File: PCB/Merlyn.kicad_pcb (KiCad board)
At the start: 2 copper layers, 35 x 35 mm, 46 parts, among them Q1 JMSL0302AU, Q10 JMSL0302AU, Q11 JMSL0302AU, Q12 JMSL0302AU, Q13 JMSL0302AU, Q14 JMSL0302AU, Q15 JMSL0302AU, Q16 JMSL0302AU, Q17 JMSL0302AU, Q18 JMSL0302AU, Q19 JMSL0302AU, Q2 JMSL0302AU, Q20 JMSL0302AU, Q21 JMSL0302AU, Q22 JMSL0302AU, Q23 JMSL0302AU, Q24 JMSL0302AU, Q3 JMSL0302AU, Q4 JMSL0302AU, Q5 JMSL0302AU, Q6 JMSL0302AU, Q7 JMSL0302AU, Q8 JMSL0302AU, Q9 JMSL0302AU, U1 AT32F435CGU7, U10 JSM6288Q, U11 EFM8BB21F16G-C-QFN20, U12 EFM8BB21F16G-C-QFN20, U13 EFM8BB21F16G-C-QFN20, U14 JSM6288Q, U15 JSM6288Q, U16 JSM6288Q, U17 MPU6500, U2 ESP8285H16, U3 LMR51420YDDCR, U4 SPX3819M5-L-3-3/TR, U5 SX1281IMLTRT, U6 W25Q128JVPIM TR, U7 APH0420T4R7M, U8 AT7456E, U9 EFM8BB21F16G-C-QFN20, X1 TAXM8M4RDBCCT2T, X2 7D027000I01, X3 XL7EL89CMI-111YLC-26M, X4 XC21M4-52.000-F10NNHPL

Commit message: routing checkpoint
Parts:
- removed Q10, Q11, Q12, Q13, Q14, Q15, Q16, Q17, Q18, Q19, Q2, Q20, Q21, Q22, Q23, Q24, Q3, Q4, Q5, Q6, Q7, Q8, Q9: JMSL0302AU, easyeda2kicad:DFN-8_L3.2-W3.1-P0.65-LS3.4-BL
- removed U10, U14, U15, U16: JSM6288Q, easyeda2kicad:VQFN-24_L4.0-W4.0-P0.50-TL-EP2.7
- removed U11, U12, U13, U9: EFM8BB21F16G-C-QFN20, easyeda2kicad:QFN-20_L3.0-W3.0-P0.50-BL-EP1.7_EFM8BB21F16G
- added C1: 0.1uF, Capacitor_SMD:C_0402_1005Metric, F.Cu at (77.3, 52.4)
- added C10: 0.1uF, Capacitor_SMD:C_0402_1005Metric, F.Cu at (137.2, 74.8)
- added C11: 0.1uF, Capacitor_SMD:C_0402_1005Metric, F.Cu at (137.2, 76.4)
- added C12: 10uF, Capacitor_SMD:C_0402_1005Metric, F.Cu at (77.3, 64.2)
- added C13: 0.1uF, Capacitor_SMD:C_0402_1005Metric, F.Cu at (77.3, 66.2)
- added C14: 0.1uF, Capacitor_SMD:C_0402_1005Metric, F.Cu at (80.2, 52.4)
- added C15: 0.1uF, Capacitor_SMD:C_0402_1005Metric, F.Cu at (80.2, 54.4)
- added C16: 10pF, Capacitor_SMD:C_0402_1005Metric, F.Cu at (80.2, 56.4)
- added C17: 10pF, Capacitor_SMD:C_0402_1005Metric, F.Cu at (80.2, 58.3)
- added C18: 10nF, Capacitor_SMD:C_0402_1005Metric, F.Cu at (143.9, 81.8)
- added C19: 0.1uF, Capacitor_SMD:C_0402_1005Metric, F.Cu at (80.2, 62.3)
- added C2: 10uF, Capacitor_SMD:C_0603_1608Metric, F.Cu at (89.4, 52.7)
- added C20: 10nF, Capacitor_SMD:C_0402_1005Metric, F.Cu at (144.4, 80.7)
- added C21: 470nF, Capacitor_SMD:C_0402_1005Metric, F.Cu at (146.6, 81.8)
- added C22: 0.1uF, Capacitor_SMD:C_0402_1005Metric, F.Cu at (83.1, 52.4)
- added C23: 10uF, Capacitor_SMD:C_0402_1005Metric, F.Cu at (83.1, 54.4)
- added C24: 0.1uF, Capacitor_SMD:C_0402_1005Metric, F.Cu at (83.1, 56.4)
- added C25: 0.1uF, Capacitor_SMD:C_0402_1005Metric, F.Cu at (145.7, 67.8)
- added C26: 0.1uF, Capacitor_SMD:C_0402_1005Metric, F.Cu at (138.0, 60.7)
- added C27: 22uF, Capacitor_SMD:C_0805_2012Metric, F.Cu at (145.8, 62.0)
- added C28: 22uF, Capacitor_SMD:C_0805_2012Metric, F.Cu at (148.5, 67.5)
- added C29: 0.1uF, Capacitor_SMD:C_0402_1005Metric, F.Cu at (145.2, 64.8)
- added C3: 10uF, Capacitor_SMD:C_0603_1608Metric, F.Cu at (89.4, 55.2)
- added C30: 0.1uF, Capacitor_SMD:C_0402_1005Metric, F.Cu at (145.7, 66.7)
- added C31: 10pF, Capacitor_SMD:C_0402_1005Metric, F.Cu at (128.5, 79.9)
- added C32: 10pF, Capacitor_SMD:C_0402_1005Metric, F.Cu at (133.6, 79.9)
- added C33: 0.1uF, Capacitor_SMD:C_0402_1005Metric, F.Cu at (134.0, 78.3)
- added C34: 0.1uF, Capacitor_SMD:C_0402_1005Metric, F.Cu at (127.2, 76.0)
- added C35: 0.1uF, Capacitor_SMD:C_0402_1005Metric, F.Cu at (128.9, 69.3)
- added C36: 0.1uF, Capacitor_SMD:C_0402_1005Metric, F.Cu at (136.0, 70.3)
- added C37: 0.1uF, Capacitor_SMD:C_0402_1005Metric, F.Cu at (85.9, 62.3)
- added C38: 10uF, Capacitor_SMD:C_0402_1005Metric, F.Cu at (85.9, 64.2)
- added C39: 0.1uF, Capacitor_SMD:C_0402_1005Metric, F.Cu at (85.9, 66.2)
- added C4: 4.7uF, Capacitor_SMD:C_1206_3216Metric, F.Cu at (83.3, 80.1)
- added C40: 0.1uF, Capacitor_SMD:C_0402_1005Metric, F.Cu at (104.8, 61.5)
- added C41: 0.1uF, Capacitor_SMD:C_0402_1005Metric, F.Cu at (104.8, 63.4)
- added C5: 0.1uF, Capacitor_SMD:C_0402_1005Metric, F.Cu at (77.3, 54.4)
- added C6: 10uF, Capacitor_SMD:C_0603_1608Metric, F.Cu at (89.4, 57.7)
- added C7: 10uF, Capacitor_SMD:C_0603_1608Metric, F.Cu at (89.4, 60.2)
- added C8: 10nF, Capacitor_SMD:C_0402_1005Metric, F.Cu at (77.3, 56.4)
- added C9: 10nF, Capacitor_SMD:C_0402_1005Metric, F.Cu at (139.3, 76.4)
- added D1: USBLC6-2SC6, easyeda2kicad:SOT-23-6_L2.9-W1.6-P0.95-LS2.8-BL, B.Cu at (78.3, 80.6)
- added D2: RED, easyeda2kicad:LED0805-RD, F.Cu at (109.0, 65.0)
- added D3: GREEN, easyeda2kicad:LED0805-R-RD, F.Cu at (109.1, 61.7)
- added D4: 1N4148W, Diode_SMD:D_SOD-123, B.Cu at (83.4, 83.5)
- added FL1: 2450FM07D0034T, easyeda2kicad:FIL_2450FM07D0034T, F.Cu at (141.1, 83.4)
- added H1: ~, easyeda2kicad:Buzzer Pad, F.Cu at (120.2, 61.4)
- added H2: ~, easyeda2kicad:JST_SH_SM08B-SRSS-TB_1x08-1MP_P1.00mm_Horizontal, F.Cu at (149.9, 74.2)
- added H3: ~, easyeda2kicad:Camera Pad, F.Cu at (142.0, 59.9)
- added J1: Conn_Coaxial_Small, easyeda2kicad:UFL, F.Cu at (144.2, 84.8)
- added R10: 5.1k, Resistor_SMD:R_0402_1005Metric, F.Cu at (95.7, 60.4)
- added R11: 5.1k, Resistor_SMD:R_0402_1005Metric, F.Cu at (98.6, 52.4)
- added R12: 75, Resistor_SMD:R_0402_1005Metric, F.Cu at (138.0, 59.6)
- added R13: 75, Resistor_SMD:R_0402_1005Metric, F.Cu at (147.5, 60.4)
- added R14: 12k, Resistor_SMD:R_0402_1005Metric, F.Cu at (98.6, 58.4)
- added R15: 12k, Resistor_SMD:R_0402_1005Metric, F.Cu at (98.6, 60.4)
- added R16: 12k, Resistor_SMD:R_0402_1005Metric, F.Cu at (101.6, 52.4)
- added R17: 5.1k, Resistor_SMD:R_0402_1005Metric, F.Cu at (101.6, 54.4)
- added R18: 5.1k, Resistor_SMD:R_0402_1005Metric, F.Cu at (101.6, 56.4)
- added R19: 12k, Resistor_SMD:R_0402_1005Metric, F.Cu at (101.6, 58.4)
- added R2: 15k, Resistor_SMD:R_0402_1005Metric, F.Cu at (92.8, 54.4)
- added R20: 1.5k, Resistor_SMD:R_0402_1005Metric, F.Cu at (101.6, 60.4)
- added R21: 5.1k, Resistor_SMD:R_0402_1005Metric, F.Cu at (129.5, 67.2)
- added R22: 5.1k, Resistor_SMD:R_0402_1005Metric, F.Cu at (131.6, 67.0)
- added R3: 2k, Resistor_SMD:R_0402_1005Metric, F.Cu at (92.8, 56.4)
- added R4: 12k, Resistor_SMD:R_0402_1005Metric, F.Cu at (92.8, 58.4)
- added R5: 0, Resistor_SMD:R_0402_1005Metric, F.Cu at (92.8, 60.4)
- added R6: 12k, Resistor_SMD:R_0402_1005Metric, F.Cu at (95.7, 52.4)
- added R7: 0, Resistor_SMD:R_0402_1005Metric, F.Cu at (95.7, 54.4)
- added R8: 12k, Resistor_SMD:R_0402_1005Metric, F.Cu at (95.7, 56.4)
- added R9: 12k, Resistor_SMD:R_0402_1005Metric, F.Cu at (95.7, 58.4)
- added REF**: MountingHole, easyeda2kicad:MountingHole, F.Cu at (129.5, 84.0)
- added REF**: MountingHole, easyeda2kicad:MountingHole, F.Cu at (149.5, 64.0)
- added REF**: MountingHole, easyeda2kicad:MountingHole, F.Cu at (149.5, 84.0)
- added REF**: MountingHole, easyeda2kicad:MountingHole, F.Cu at (129.5, 64.0)
- added U18: LMR51420, easyeda2kicad:SOT-23-6_L2.9-W1.6-P0.95-LS2.9-BL, F.Cu at (109.1, 77.9)
- added USB1: TYPE-C 16PIN 2MD(073), easyeda2kicad:USB-C-SMD_TYPE-C-6PIN-2MD-073, B.Cu at (125.8, 51.3)
- Q1: value JMSL0302AU -> 2N7002; footprint easyeda2kicad:DFN-8_L3.2-W3.1-P0.65-LS3.4-BL -> Package_TO_SOT_SMD:SOT-23
- R1: value HOYLR2512E-3W-0.5MR-1% -> 12k; footprint easyeda2kicad:R2512 -> Resistor_SMD:R_0402_1005Metric; moved to F.Cu
- U3: value LMR51420YDDCR -> W25Q128JVSIQTR; footprint easyeda2kicad:SOT-23-6_L2.9-W1.6-P0.95-LS2.9-BL -> easyeda2kicad:SOIC-8_L5.3-W5.3-P1.27-LS8.0-BL; moved to B.Cu
- U4: value SPX3819M5-L-3-3/TR -> SPX3819; moved to B.Cu
- U6: value W25Q128JVPIM TR -> BMP388; footprint easyeda2kicad:WSON-8_L6.0-W5.0-P1.27-BL-EP -> easyeda2kicad:LGA-10_L2.0-W2.0-P0.50-BL
- U7: value APH0420T4R7M -> 4.7uH
- X1: value TAXM8M4RDBCCT2T -> 8MHz
- X2: value 7D027000I01 -> 27MHz
- X3: value XL7EL89CMI-111YLC-26M -> 26MHz
- X4: value XC21M4-52.000-F10NNHPL -> 52MHz
- moved Q1 45.4 mm to (108.9, 72.2), turned to 180 degrees
- moved R1 42.7 mm to (92.8, 52.4)
- moved U7 29.9 mm to (103.4, 78.5)
- moved X3 23.3 mm to (136.2, 80.8)
- moved U8 21.6 mm to (140.8, 66.1), turned to -90 degrees
- moved X4 19.1 mm to (146.5, 79.9), turned to 90 degrees
- moved U5 16.8 mm to (140.8, 79.9), turned to 180 degrees
- moved U2 16.7 mm to (135.6, 85.6)
- moved X2 14.8 mm to (135.7, 64.7), turned to 90 degrees
- moved U1 13.1 mm to (131.6, 73.7), turned to 90 degrees
- moved U6 12.2 mm to (133.3, 64.7)
- moved U4 9.40 mm to (133.0, 72.4), turned to 180 degrees
- moved U17 7.66 mm to (139.5, 74.0), turned to 180 degrees
- moved U3 1.91 mm to (127.8, 75.4), turned to 180 degrees
- moved X1 0.76 mm to (131.0, 80.0), turned to 180 degrees
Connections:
- Q1 pad 1: unconnected-(Q1-S-Pad1) -> Net-(Q1-G)
- Q1 pad 2: unconnected-(Q1-S-Pad2) -> GND
- Q1 pad 3: unconnected-(Q1-S-Pad3) -> Net-(D4-A)
- R1 pad 1: unconnected-(R1-Pad1) -> +3V3
- R1 pad 2: unconnected-(R1-Pad2) -> NRST
- U1 pad 1: unconnected-(U1-VBAT-Pad1) -> +3V3
- U1 pad 10: unconnected-(U1-PA0-Pad10) -> ADC_VOL
- U1 pad 11: unconnected-(U1-PA1-Pad11) -> ADC_CUR
- U1 pad 12: unconnected-(U1-PA2-Pad12) -> UART2_TX
- U1 pad 13: unconnected-(U1-PA3-Pad13) -> UART2_RX
- U1 pad 14: unconnected-(U1-PA4-Pad14) -> SPI1_CS
- U1 pad 15: unconnected-(U1-PA5-Pad15) -> SPI1_SCK
- U1 pad 16: unconnected-(U1-PA6-Pad16) -> SPI1_MISO
- U1 pad 17: unconnected-(U1-PA7-Pad17) -> SPI1_MOSI
- U1 pad 18: unconnected-(U1-PB0-Pad18) -> MOT3
- U1 pad 19: unconnected-(U1-PB1-Pad19) -> MOT4
- U1 pad 2: unconnected-(U1-PC13-Pad2) -> SPI2_CS2
- U1 pad 20: unconnected-(U1-PB2-Pad20) -> BOOT1
- U1 pad 21: unconnected-(U1-PB10-Pad21) -> UART3_TX
- U1 pad 22: unconnected-(U1-PB11-Pad22) -> UART3_RX
- U1 pad 23: unconnected-(U1-PH3-Pad23) -> I2C_SDA
- U1 pad 24: unconnected-(U1-VDD-Pad24) -> +3V3
- U1 pad 25: unconnected-(U1-PB12-Pad25) -> SPI2_CS1
- U1 pad 26: unconnected-(U1-PB13-Pad26) -> SPI2_SCK
- U1 pad 27: unconnected-(U1-PB14-Pad27) -> SPI2_MISO
- U1 pad 28: unconnected-(U1-PB15-Pad28) -> SPI2_MOSI
- U1 pad 29: unconnected-(U1-PA8-Pad29) -> LED
- U1 pad 30: unconnected-(U1-PA9-Pad30) -> UART1_TX
- U1 pad 31: unconnected-(U1-PA10-Pad31) -> UART1_RX
- U1 pad 32: unconnected-(U1-PA11-Pad32) -> D-
- U1 pad 33: unconnected-(U1-PA12-Pad33) -> D+
- U1 pad 34: unconnected-(U1-PA13-Pad34) -> SWDIO
- U1 pad 35: unconnected-(U1-PH2-Pad35) -> I2C_SCL
- U1 pad 36: unconnected-(U1-VDD-Pad36) -> +3V3
- U1 pad 37: unconnected-(U1-PA14-Pad37) -> SWCLK
- U1 pad 39: unconnected-(U1-PB3-Pad39) -> UART7_RX
- U1 pad 4: unconnected-(U1-PC15-Pad4) -> BEEPER
- U1 pad 40: unconnected-(U1-PB4-Pad40) -> UART7_TX
- U1 pad 42: unconnected-(U1-PB6-Pad42) -> MOT1
- U1 pad 43: unconnected-(U1-PB7-Pad43) -> MOT2
- U1 pad 44: unconnected-(U1-BOOT0-Pad44) -> BOOT0
- U1 pad 45: unconnected-(U1-PB8-Pad45) -> UART5_RX
- U1 pad 46: unconnected-(U1-PB9-Pad46) -> UART5_TX
- U1 pad 47: unconnected-(U1-VSS-Pad47) -> GND
- U1 pad 48: unconnected-(U1-VDD-Pad48) -> +3V3
- U1 pad 49: unconnected-(U1-EP-Pad49) -> GND
- U1 pad 5: unconnected-(U1-PH0-Pad5) -> Net-(U1-PH0)
- U1 pad 6: unconnected-(U1-PH1-Pad6) -> Net-(U1-PH1)
- U1 pad 7: unconnected-(U1-NRST-Pad7) -> NRST
- U1 pad 8: unconnected-(U1-VSSA/VREF--Pad8) -> GND
- U1 pad 9: unconnected-(U1-VDDA/VREF+-Pad9) -> +3V3
- U17 pad 10: unconnected-(U17-REGOUT-Pad10) -> Net-(U17-REGOUT)
- U17 pad 11: unconnected-(U17-FSYNC-Pad11) -> GND
- U17 pad 13: unconnected-(U17-VDD-Pad13) -> +3V3
- U17 pad 18: unconnected-(U17-GND-Pad18) -> GND
- U17 pad 20: unconnected-(U17-RESV-Pad20) -> GND
- U17 pad 22: unconnected-(U17-nCS-Pad22) -> SPI1_CS
- U17 pad 23: unconnected-(U17-SCL/SCLK-Pad23) -> SPI1_SCK
- U17 pad 24: unconnected-(U17-SDA/SDI-Pad24) -> SPI1_MOSI
- U17 pad 8: unconnected-(U17-VDDIO-Pad8) -> +3V3
- U17 pad 9: unconnected-(U17-SDO/AD0-Pad9) -> SPI1_MISO
- U2 pad 1: unconnected-(U2-VDDA-Pad1) -> +3V3
- U2 pad 10: unconnected-(U2-MTDI-Pad10) -> GPIO12
- U2 pad 11: unconnected-(U2-VDDPST-Pad11) -> +3V3
- U2 pad 12: unconnected-(U2-MTCK-Pad12) -> GPIO13
- U2 pad 13: unconnected-(U2-MTDO-Pad13) -> GPIO15
- U2 pad 14: unconnected-(U2-GPIO2-Pad14) -> GPIO2
- U2 pad 15: unconnected-(U2-GPIO0-Pad15) -> Net-(U2-GPIO0)
- U2 pad 16: unconnected-(U2-GPIO4-Pad16) -> GPIO4
- U2 pad 17: unconnected-(U2-VDDPST-Pad17) -> +3V3
- U2 pad 24: unconnected-(U2-GPIO5-Pad24) -> GPIO5
- U2 pad 25: unconnected-(U2-U0RXD-Pad25) -> PIN
- U2 pad 26: unconnected-(U2-U0TXD-Pad26) -> PIN
- U2 pad 27: unconnected-(U2-XTAL_OUT-Pad27) -> Net-(U2-XTAL_OUT)
- U2 pad 28: unconnected-(U2-XTAL_IN-Pad28) -> Net-(U2-XTAL_IN)
- U2 pad 29: unconnected-(U2-VDDD-Pad29) -> +3V3
- U2 pad 3: unconnected-(U2-VDD3P3-Pad3) -> +3V3
- U2 pad 30: unconnected-(U2-VDDA-Pad30) -> +3V3
- U2 pad 31: unconnected-(U2-RES12K-Pad31) -> Net-(U2-RES12K)
- U2 pad 33: unconnected-(U2-GND-Pad33) -> GND
- U2 pad 4: unconnected-(U2-VDD3P3-Pad4) -> +3V3
- U2 pad 7: unconnected-(U2-CHIP_EN-Pad7) -> Net-(U2-CHIP_EN)
- U2 pad 9: unconnected-(U2-MTMS-Pad9) -> GPIO14
- U3 pad 1: unconnected-(U3-GND-Pad1) -> PIN
- U3 pad 2: unconnected-(U3-SW-Pad2) -> PIN
- U3 pad 3: unconnected-(U3-VIN-Pad3) -> +3V3
- U3 pad 4: unconnected-(U3-FB-Pad4) -> GND
- U3 pad 5: unconnected-(U3-EN-Pad5) -> PIN
- U3 pad 6: unconnected-(U3-CB-Pad6) -> PIN
- U4 pad 1: unconnected-(U4-IN-Pad1) -> +5V
- U4 pad 2: unconnected-(U4-GND-Pad2) -> GND
- U4 pad 3: unconnected-(U4-EN-Pad3) -> +5V
- U4 pad 4: unconnected-(U4-BYP-Pad4) -> Net-(U4-BYP)
- U4 pad 5: unconnected-(U4-OUT-Pad5) -> +3V3
- U5 pad 1: unconnected-(U5-VR_PA-Pad1) -> Net-(U5-VR_PA)
- U5 pad 11: unconnected-(U5-VBAT_IO-Pad11) -> +3V3
- U5 pad 12: unconnected-(U5-DCC_FB-Pad12) -> DCC_FB
- U5 pad 13: unconnected-(U5-GND-Pad13) -> GND
- U5 pad 15: unconnected-(U5-VBAT-Pad15) -> +3V3
- U5 pad 16: unconnected-(U5-MISO_TX-Pad16) -> GPIO12
- U5 pad 17: unconnected-(U5-MOSI_RX-Pad17) -> GPIO13
- U5 pad 18: unconnected-(U5-SCK_RTSN-Pad18) -> GPIO14
- U5 pad 19: unconnected-(U5-NSS_CTS-Pad19) -> GPIO15
- U5 pad 2: unconnected-(U5-VDD_IN-Pad2) -> DCC_FB
- U5 pad 20: unconnected-(U5-GND-Pad20) -> GND
- U5 pad 21: unconnected-(U5-GND-Pad21) -> GND
- U5 pad 22: unconnected-(U5-RFIO-Pad22) -> RFOUT
- U5 pad 23: unconnected-(U5-GND-Pad23) -> GND
- U5 pad 24: unconnected-(U5-GND-Pad24) -> GND
- U5 pad 25: unconnected-(U5-EP-Pad25) -> GND
- U5 pad 3: unconnected-(U5-NRESET-Pad3) -> GPIO2
- U5 pad 4: unconnected-(U5-XTA-Pad4) -> Net-(U5-XTA)
- U5 pad 5: unconnected-(U5-GND-Pad5) -> GND
- U5 pad 6: unconnected-(U5-XTB-Pad6) -> Net-(U5-XTB)
- U5 pad 7: unconnected-(U5-BUSY-Pad7) -> GPIO5
- U5 pad 8: unconnected-(U5-DIO1-Pad8) -> GPIO4
- U6 pad 1: unconnected-(U6-/CS-Pad1) -> +3V3
- U6 pad 2: unconnected-(U6-DO(IO1)-Pad2) -> I2C_SCL
- U6 pad 3: unconnected-(U6-/WP(IO2)-Pad3) -> GND
- U6 pad 4: unconnected-(U6-GND-Pad4) -> I2C_SDA
- U6 pad 5: unconnected-(U6-DI(IO0)-Pad5) -> GND
- U6 pad 6: unconnected-(U6-CLK-Pad6) -> +3V3
- U6 pad 8: unconnected-(U6-VCC-Pad8) -> GND
- U6 pad 9: unconnected-(U6-EP-Pad9) -> GND
- U7 pad 1: unconnected-(U7-Pad1) -> Net-(U18-SW)
- U7 pad 2: unconnected-(U7-Pad2) -> +5V
- U8 pad 10: unconnected-(U8-SCLK-Pad10) -> SPI2_SCK
- U8 pad 11: unconnected-(U8-SDOUT-Pad11) -> SPI2_MISO
- U8 pad 19: unconnected-(U8-~{RESET}-Pad19) -> +5V
- U8 pad 20: unconnected-(U8-AGND-Pad20) -> GND
- U8 pad 21: unconnected-(U8-AVDD-Pad21) -> +5V
- U8 pad 22: unconnected-(U8-VIN-Pad22) -> VIN
- U8 pad 23: unconnected-(U8-PGND-Pad23) -> GND
- U8 pad 24: unconnected-(U8-PVDD-Pad24) -> +5V
- U8 pad 25: unconnected-(U8-SAG-Pad25) -> Net-(U8-SAG)
- U8 pad 26: unconnected-(U8-VOUT-Pad26) -> Net-(U8-VOUT)
- U8 pad 29: unconnected-(U8-EP-Pad29) -> GND
- U8 pad 3: unconnected-(U8-DVDD-Pad3) -> +5V
- U8 pad 4: unconnected-(U8-DGND-Pad4) -> GND
- U8 pad 5: unconnected-(U8-CLKIN-Pad5) -> Net-(U8-CLKIN)
- U8 pad 6: unconnected-(U8-XFB-Pad6) -> Net-(U8-XFB)
- U8 pad 8: unconnected-(U8-~{CS}-Pad8) -> SPI2_CS1
- U8 pad 9: unconnected-(U8-SDIN-Pad9) -> SPI2_MOSI
- X1 pad 1: unconnected-(X1-Pad1) -> Net-(U1-PH1)
- X1 pad 2: unconnected-(X1-Pad2) -> GND
- X1 pad 3: unconnected-(X1-Pad3) -> Net-(U1-PH0)
- X1 pad 4: unconnected-(X1-Pad4) -> GND
- X2 pad 1: unconnected-(X2-Pad1) -> Net-(U8-XFB)
- X2 pad 2: unconnected-(X2-GND-Pad2) -> GND
- X2 pad 3: unconnected-(X2-Pad3) -> Net-(U8-CLKIN)
- X2 pad 4: unconnected-(X2-GND-Pad4) -> GND
- X3 pad 1: unconnected-(X3-Pad1) -> Net-(U2-XTAL_IN)
- X3 pad 2: unconnected-(X3-GND-Pad2) -> GND
- X3 pad 3: unconnected-(X3-Pad3) -> Net-(U2-XTAL_OUT)
- X3 pad 4: unconnected-(X3-GND-Pad4) -> GND
- X4 pad 1: unconnected-(X4-Pad1) -> Net-(U5-XTA)
- X4 pad 2: unconnected-(X4-GND-Pad2) -> GND
- X4 pad 3: unconnected-(X4-Pad3) -> Net-(U5-XTB)
- X4 pad 4: unconnected-(X4-GND-Pad4) -> GND
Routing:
- net GND: track 0.00 -> 33.3 mm, vias 0 -> 45
- net DCC_FB: track 0.00 -> 13.0 mm, vias 0 -> 2
- net +3V3: track 0.00 -> 10.6 mm, vias 0 -> 5
- net Net-(C27-Pad1): track 0.00 -> 9.67 mm
- net SPI1_SCK: track 0.00 -> 9.08 mm, vias 0 -> 2
- net VIN: track 0.00 -> 8.98 mm
- net SPI1_CS: track 0.00 -> 8.94 mm, vias 0 -> 2
- net SPI1_MOSI: track 0.00 -> 8.61 mm, vias 0 -> 2
- net SPI2_MOSI: track 0.00 -> 7.35 mm
- net SPI2_CS1: track 0.00 -> 6.83 mm, vias 0 -> 2
- net Net-(U8-SAG): track 0.00 -> 6.73 mm
- net SPI2_MISO: track 0.00 -> 6.35 mm
- net +5V: track 0.00 -> 6.15 mm
- net SPI2_SCK: track 0.00 -> 6.13 mm, vias 0 -> 2
- net Net-(U1-PH0): track 0.00 -> 6.04 mm
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- added copper zone on In1.Cu, net +3V3
- added copper zone on B.Cu, net GND
- added copper zone on F.Cu, net GND
- added copper zone on In2.Cu, net GND
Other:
- board size 35 x 35 mm -> 30.5 x 30.5 mm
- copper layers 2 -> 4

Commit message: checkpoint
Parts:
- C2, C3, C4, R5, R7, U7: moved to B.Cu
- H2: footprint easyeda2kicad:JST_SH_SM08B-SRSS-TB_1x08-1MP_P1.00mm_Horizontal -> easyeda2kicad:ESC Header
- USB1: footprint easyeda2kicad:USB-C-SMD_TYPE-C-6PIN-2MD-073 -> easyeda2kicad:USB-TYPE-C-SMD_TYPE-C-16P-QTWT
- moved C23 69.5 mm to (151.3, 67.7)
- moved C24 69.0 mm to (151.3, 66.7)
- moved D1 64.8 mm to (142.2, 69.5), turned to -90 degrees
- moved C19 62.8 mm to (141.3, 76.4), turned to -135 degrees
- moved C14 61.3 mm to (131.4, 86.1), turned to 45 degrees
- moved C22 60.5 mm to (137.9, 78.0), turned to -90 degrees
- moved C15 60.2 mm to (134.1, 81.2), turned to 180 degrees
- moved C17 59.7 mm to (136.4, 78.4)
- moved C16 59.2 mm to (134.6, 79.7), turned to -90 degrees
- moved C5 58.6 mm to (135.7, 59.5)
- moved R11 57.7 mm to (149.2, 80.2)
- moved R10 57.4 mm to (149.2, 81.2)
- moved C1 56.0 mm to (132.4, 62.5), turned to 90 degrees
- moved R7 53.9 mm to (137.8, 88.2)
- moved R8 52.9 mm to (139.2, 86.6), turned to -90 degrees
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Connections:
- D1 pad 1: DIN+ -> DIN-
- D1 pad 3: DIN- -> DIN+
- D1 pad 4: D- -> D+
- D1 pad 6: D+ -> D-
- R16 pad 2: PIN -> SPI2_CS2
- U2 pad 25: PIN -> UART2_TX
- U2 pad 26: PIN -> UART2_RX
- U3 pad 1: PIN -> SPI2_CS2
- U3 pad 2: PIN -> SPI2_MISO
- U3 pad 5: PIN -> SPI2_MOSI
- U3 pad 6: PIN -> SPI2_SCK
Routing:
- net +3V3: track 10.6 -> 52.2 mm, vias 5 -> 14
- net +5V: track 6.15 -> 47.5 mm, vias 0 -> 6
- net SPI2_CS2: track 0.00 -> 25.1 mm, vias 0 -> 2
- net GPIO4: track 0.00 -> 18.5 mm, vias 0 -> 2
- net GND: track 33.3 -> 50.3 mm, vias 45 -> 72
- net VBAT: track 0.00 -> 14.0 mm, vias 0 -> 3
- net GPIO15: track 0.00 -> 13.8 mm, vias 0 -> 2
- net Net-(USB1-CC1): track 0.00 -> 13.5 mm, vias 0 -> 1
- net GPIO12: track 0.00 -> 13.4 mm, vias 0 -> 2
- net GPIO2: track 1.60 -> 15.0 mm, vias 1 -> 2
- net D+: track 0.00 -> 12.7 mm, vias 0 -> 1
- net D-: track 0.00 -> 12.7 mm, vias 0 -> 1
- net GPIO5: track 0.00 -> 12.4 mm, vias 0 -> 2
- net SPI2_MISO: track 6.35 -> 18.0 mm, vias 0 -> 1
- net GPIO13: track 0.00 -> 11.6 mm, vias 0 -> 2
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- added copper zone on In2.Cu, net +3V3
- added copper zone on In1.Cu, net GND
- removed copper zone on In1.Cu, net +3V3
- removed copper zone on In2.Cu, net GND

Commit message: checkpoint
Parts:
- added C42: 0.1uF, Capacitor_SMD:C_0402_1005Metric, F.Cu at (145.5, 74.7)
- added H4: ~, easyeda2kicad:VTX Pad, B.Cu at (142.8, 59.9)
- added R23: 91k, Resistor_SMD:R_0603_1608Metric, F.Cu at (144.9, 76.0)
- added R25: 12k, Resistor_SMD:R_0402_1005Metric, F.Cu at (144.1, 74.3)
- moved C39 66.8 mm to (152.7, 67.2), turned to 90 degrees
- moved C38 66.4 mm to (152.3, 65.7), turned to 180 degrees
- moved C8 65.5 mm to (141.1, 71.5), turned to 180 degrees
- moved C6 59.0 mm to (144.9, 77.5), turned to 180 degrees
- moved R17 58.0 mm to (152.4, 82.3)
- moved C7 56.3 mm to (144.6, 71.5), turned to 180 degrees
- moved R16 54.3 mm to (153.8, 67.5), turned to 90 degrees
- moved R1 47.2 mm to (132.5, 77.9), turned to 180 degrees
- moved C37 46.7 mm to (129.9, 77.9), turned to 180 degrees
- moved D2 44.3 mm to (152.4, 80.9)
- moved R15 38.6 mm to (135.9, 70.1)
- moved R14 36.0 mm to (127.5, 79.9), turned to -90 degrees
- moved D4 32.7 mm to (116.0, 86.0)
- moved C40 25.5 mm to (129.7, 66.8)
- moved C41 25.3 mm to (129.7, 67.8)
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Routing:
- net VBAT: track 14.0 -> 57.0 mm, vias 3 -> 4
- net +5V: track 47.5 -> 71.2 mm, vias 6 -> 7
- net UART1_TX: track 0.00 -> 19.0 mm, vias 0 -> 2
- net ADC_CUR: track 0.00 -> 17.7 mm, vias 0 -> 2
- net +3V3: track 52.2 -> 69.4 mm, vias 14 -> 19
- net ADC_VOL: track 0.00 -> 15.3 mm, vias 0 -> 2
- net SPI2_CS2: track 25.1 -> 39.1 mm, vias 2 -> 3
- net GND: track 50.3 -> 60.0 mm, vias 72 -> 73
- net NRST: track 0.00 -> 7.91 mm, vias 0 -> 2
- net BOOT0: track 0.00 -> 7.84 mm, vias 0 -> 2
- net VIDOUT: track 0.00 -> 5.21 mm, vias 0 -> 1
- net BOOT1: track 0.00 -> 5.17 mm, vias 0 -> 2
- net Net-(U4-BYP): track 0.00 -> 5.14 mm, vias 0 -> 1
- net Net-(D2-+): track 0.00 -> 1.66 mm
- net D+: track 12.7 -> 14.3 mm
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
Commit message: polka dots
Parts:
- added H10: ~, easyeda2kicad:SWCLK TP, B.Cu at (127.6, 71.0)
- added H11: ~, easyeda2kicad:SWDIO TP, B.Cu at (131.1, 71.3)
- added H12: ~, easyeda2kicad:SWD_BOOT TP, B.Cu at (129.5, 74.8)
- added H13: ~, easyeda2kicad:SWD_RST TP, B.Cu at (128.4, 78.7)
- added H14: ~, easyeda2kicad:Power Pad, B.Cu at (153.7, 80.3)
- added H5: ~, easyeda2kicad:GPS Pad, F.Cu at (125.3, 68.4)
- added H6: ~, easyeda2kicad:UART5 PAD, F.Cu at (125.3, 78.7)
- added H7: ~, easyeda2kicad:UART3 PAD, B.Cu at (125.3, 74.8)
- added H8: ~, easyeda2kicad:ELRS_RX TP, B.Cu at (134.4, 76.0)
- added H9: ~, easyeda2kicad:ELRS_TX TP, B.Cu at (135.2, 76.8)
- H1, R19, R20: moved to B.Cu
- moved D4 20.4 mm to (135.3, 79.6)
- moved R19 19.2 mm to (135.7, 77.9)
- moved C12 18.3 mm to (140.6, 87.5), turned to 180 degrees
- moved C13 17.4 mm to (139.5, 88.4), turned to 180 degrees
- moved H1 17.0 mm to (125.3, 81.0), turned to 90 degrees
- moved R20 16.9 mm to (133.8, 77.0), turned to 135 degrees
- moved Q1 12.5 mm to (130.6, 78.0)
- moved R18 10.5 mm to (127.4, 69.5), turned to 90 degrees
- moved D3 0.11 mm to (128.0, 67.2), turned to -90 degrees
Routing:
- net +5V: track 71.2 -> 127.1 mm, vias 7 -> 10
- net +3V3: track 69.4 -> 101.3 mm, vias 19 -> 21
- net MOT2: track 0.00 -> 29.2 mm, vias 0 -> 2
- net MOT1: track 0.00 -> 27.3 mm, vias 0 -> 2
- net MOT4: track 0.00 -> 22.6 mm
- net MOT3: track 0.00 -> 21.1 mm
- net GND: track 60.0 -> 75.6 mm, vias 73 -> 79
- net UART3_TX: track 0.00 -> 14.6 mm, vias 0 -> 1
- net UART3_RX: track 0.00 -> 14.3 mm, vias 0 -> 1
- net Net-(D4-A): track 0.00 -> 10.3 mm
- net LED: track 0.00 -> 8.96 mm, vias 0 -> 2
- net I2C_SDA: track 8.00 -> 16.5 mm, vias 2 -> 3
- net I2C_SCL: track 6.67 -> 14.1 mm, vias 0 -> 2
- net UART5_RX: track 0.00 -> 6.42 mm, vias 0 -> 2
- net ADC_CUR: track 17.7 -> 23.6 mm
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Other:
- board text added: "BOOT"
- board text added: "RST"

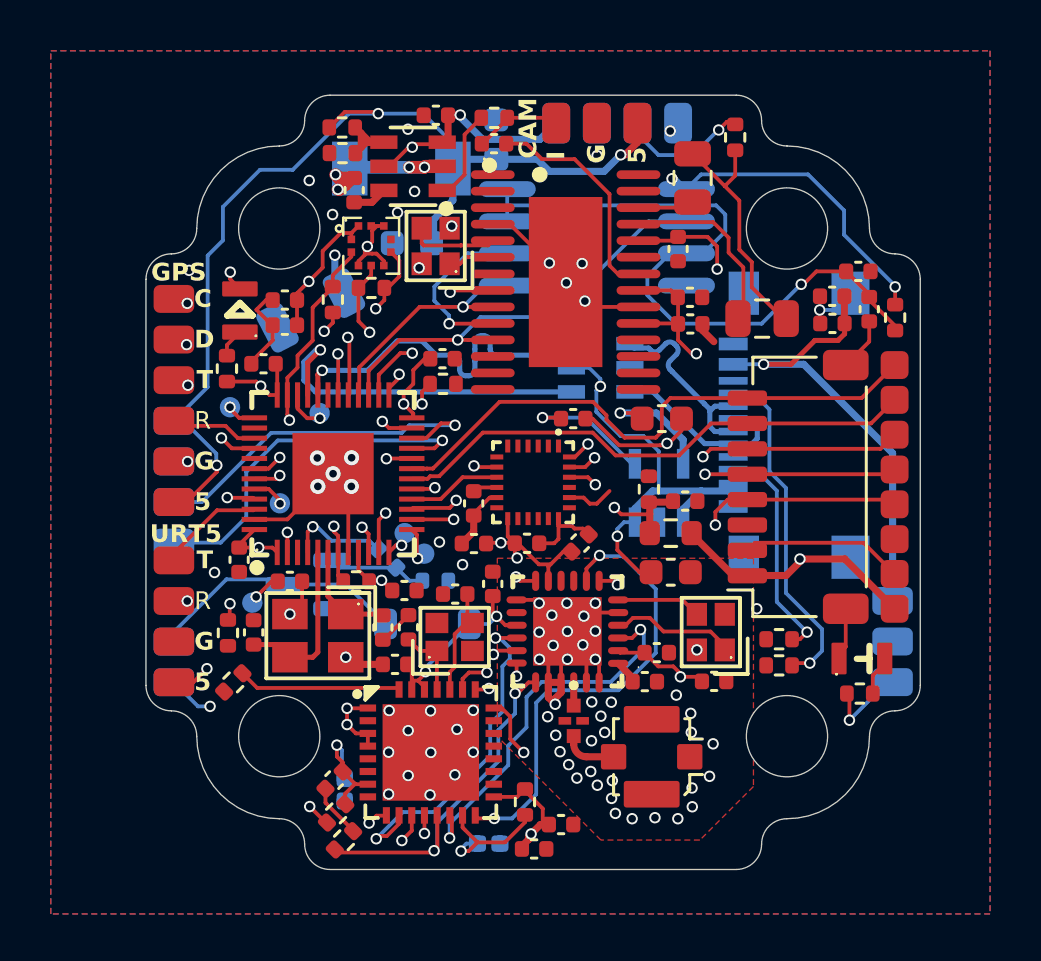
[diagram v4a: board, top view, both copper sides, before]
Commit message: completed flight controller
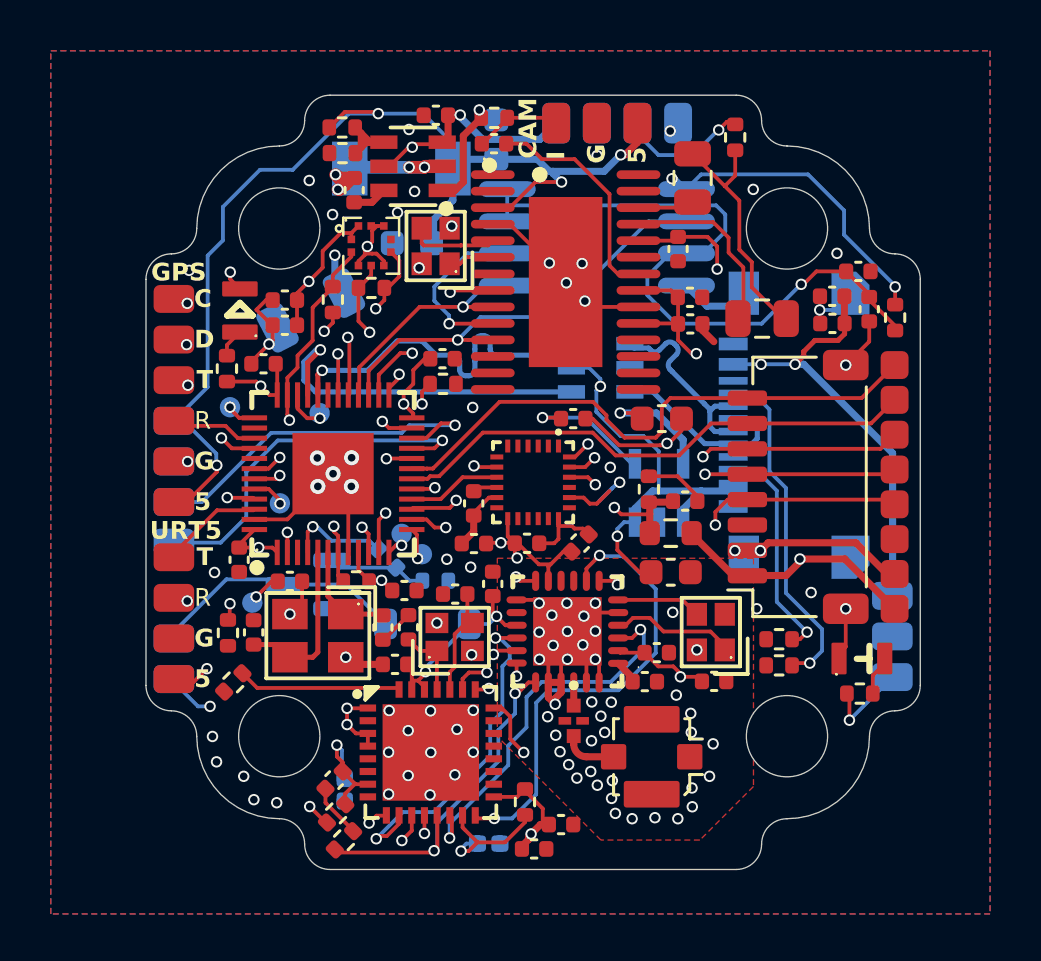
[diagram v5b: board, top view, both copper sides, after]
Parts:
- moved H14 0.20 mm to (153.7, 80.1)
- moved H1 0.12 mm to (125.3, 80.8)
- moved H6 0.12 mm to (125.3, 78.5)
- moved H8 0.12 mm to (134.3, 76.0)
- moved H9 0.09 mm to (135.1, 76.8)
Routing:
- net GND: track 75.6 -> 84.9 mm, vias 79 -> 99
- net +5V: track 127.1 -> 130.7 mm, vias 10 -> 12
- net VBAT: track 57.0 -> 58.8 mm
- net UART2_RX: track 9.23 -> 9.74 mm
- net MOT2: track 29.2 -> 29.7 mm
